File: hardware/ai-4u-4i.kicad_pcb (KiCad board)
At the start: 4 copper layers, 100 x 85 mm, 207 parts, among them J101 TNG-Power-TOP, J102 TNG-Power-BTM, J103 TNG-Data-TOP, J104 TNG-Data-BTM, P102 Debug, P103 PE, P201 INPUT0, P202 INPUT1, P203 INPUT2, P204 INPUT3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

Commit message: fix values
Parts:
- C127, C128: value 4.7nF/2kV -> 1nF/2kV
- R101: value 510 -> 1k

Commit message: specify value
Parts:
- C115: value TBD -> 2.2uF

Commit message: specify value
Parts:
- R253: value TBD -> 1k

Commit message: part specification
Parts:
- R256, R257: value TBD -> DNP

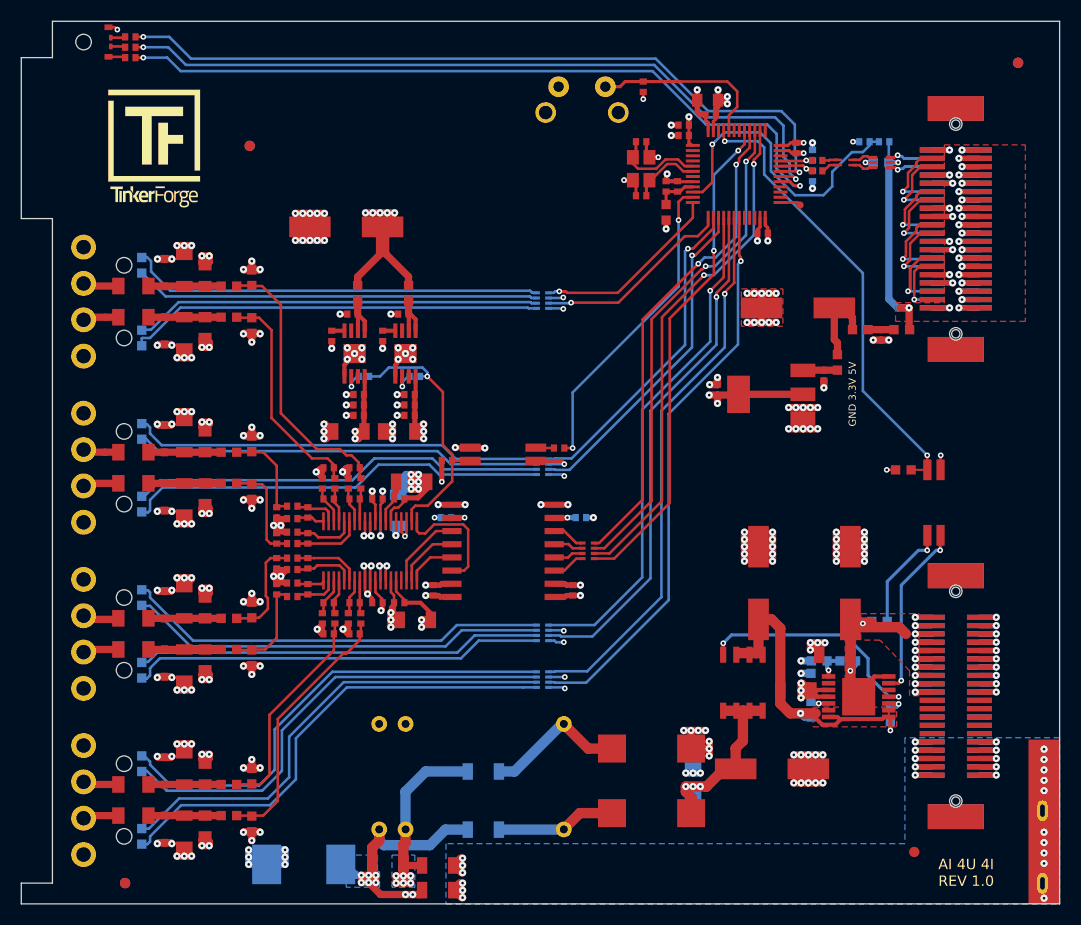
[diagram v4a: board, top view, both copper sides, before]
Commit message: add version 1.1  * fix footprints, improve routing
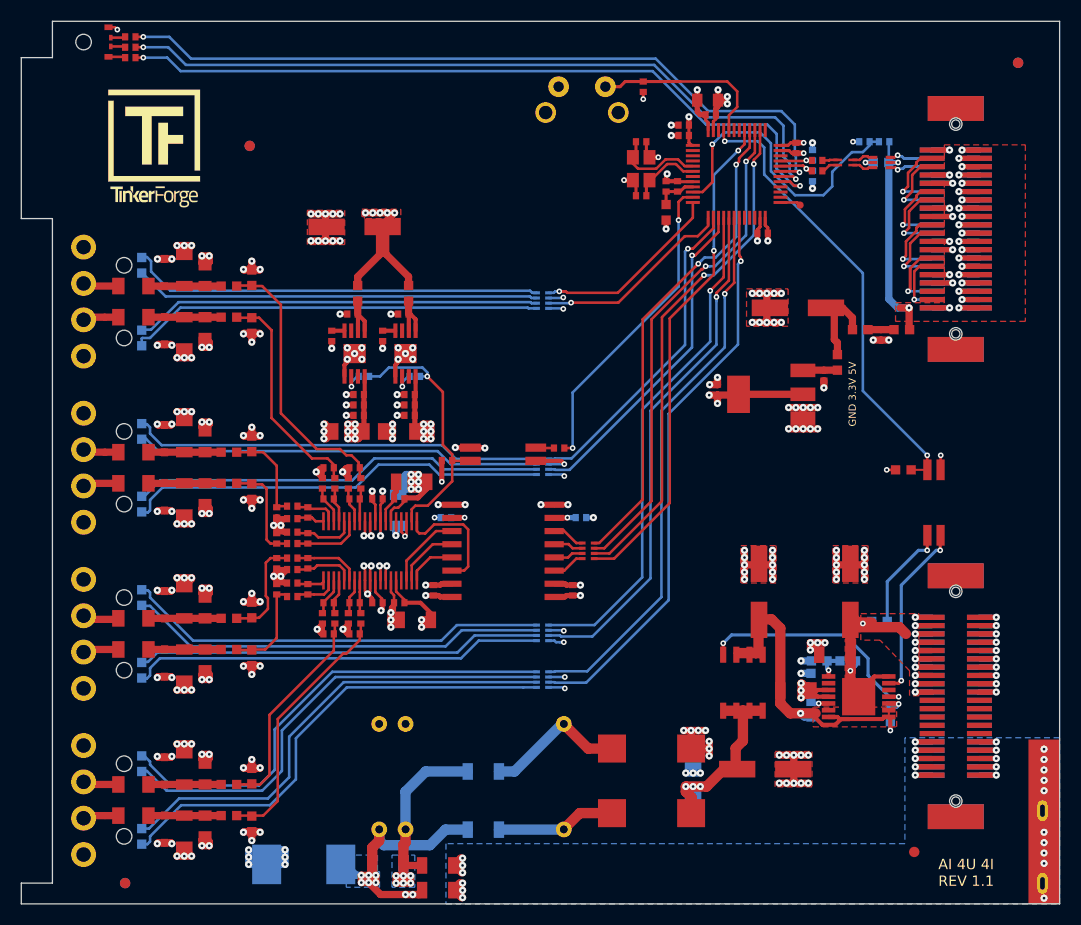
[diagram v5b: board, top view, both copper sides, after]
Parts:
- C108, C109: value TBD -> 33pF
- C111: value TBD -> 100µF; footprint kicad-libraries:ELKO_83 -> kicad-libraries:ELKO_63
- C122, C123, C124, C234: footprint kicad-libraries:ELKO_83 -> kicad-libraries:ELKO_63
- X101: value TBD -> 8MHz
- moved C124 0.85 mm to (160.8, 117.5)
- moved C122 0.85 mm to (169.7, 117.5)
- moved C234 0.80 mm to (121.9, 82.3)
- moved C123 0.65 mm to (161.4, 134.5)
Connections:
- J101 pad 21: (no net) -> Net-(J101-Pad21)
- J101 pad 22: (no net) -> Net-(J101-Pad22)
- J101 pad 23: (no net) -> Net-(J101-Pad23)
- J101 pad 24: (no net) -> Net-(J101-Pad24)
- J101 pad 25: (no net) -> Net-(J101-Pad25)
- J101 pad 26: (no net) -> Net-(J101-Pad26)
- J101 pad 27: (no net) -> Net-(J101-Pad27)
- J101 pad 28: (no net) -> Net-(J101-Pad28)
- J101 pad 29: (no net) -> Net-(J101-Pad29)
- J101 pad 30: (no net) -> Net-(J101-Pad30)
- J102 pad 21: (no net) -> Net-(J102-Pad21)
- J102 pad 22: (no net) -> Net-(J102-Pad22)
- J102 pad 23: (no net) -> Net-(J102-Pad23)
- J102 pad 24: (no net) -> Net-(J102-Pad24)
- J102 pad 25: (no net) -> Net-(J102-Pad25)
- J102 pad 26: (no net) -> Net-(J102-Pad26)
- J102 pad 27: (no net) -> Net-(J102-Pad27)
- J102 pad 28: (no net) -> Net-(J102-Pad28)
- J102 pad 29: (no net) -> Net-(J102-Pad29)
- J102 pad 30: (no net) -> Net-(J102-Pad30)
- J103 pad 35: (no net) -> Net-(J103-Pad35)
- J103 pad 37: (no net) -> Net-(J103-Pad37)
- U101 pad 2: (no net) -> Net-(U101-Pad2)
- U101 pad 20: (no net) -> Net-(U101-Pad20)
- U101 pad 21: (no net) -> Net-(U101-Pad21)
- U101 pad 22: (no net) -> Net-(U101-Pad22)
- U101 pad 26: (no net) -> Net-(U101-Pad26)
- U101 pad 27: (no net) -> Net-(U101-Pad27)
- U101 pad 28: (no net) -> Net-(U101-Pad28)
- U101 pad 3: (no net) -> Net-(U101-Pad3)
- U101 pad 34: (no net) -> Net-(U101-Pad34)
- U101 pad 37: (no net) -> Net-(U101-Pad37)
- U101 pad 4: (no net) -> Net-(U101-Pad4)
- U101 pad 42: (no net) -> Net-(U101-Pad42)
- U101 pad 43: (no net) -> Net-(U101-Pad43)
- U101 pad 46: (no net) -> Net-(U101-Pad46)
- U101 pad 7: (no net) -> Net-(U101-Pad7)
- U104 pad 7: (no net) -> Net-(U104-Pad7)
- U104 pad 8: (no net) -> Net-(U104-Pad8)
- U106 pad 12: (no net) -> Net-(U106-Pad12)
- U106 pad 2: (no net) -> Net-(U106-Pad2)
- U201 pad 35: (no net) -> Net-(U201-Pad35)
- U204 pad 3: (no net) -> Net-(U204-Pad3)
- U204 pad 7: (no net) -> Net-(U204-Pad7)
- U205 pad 3: (no net) -> Net-(U205-Pad3)
- U205 pad 7: (no net) -> Net-(U205-Pad7)
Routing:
- net AVDD: track 35.7 -> 41.1 mm, vias 4 -> 8
- net DVDD: track 45.2 -> 48.7 mm, vias 8 -> 11
- added copper zone on F.Cu, net AGND
- added copper zone on VCC, net AVDD
- added copper zone on VCC, net DVDD
- added copper zone on F.Cu, net VCC
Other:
- board text added: "AI 4U 4I REV 1.1"
- board text added: "Copyright Tinkerforge GmbH 2020. This documentation describes Open Hardware and is licensed under the CERN OHL v. 1.1. You may redistribute and modify this documentation under the terms of the CERN OHL v.1.1. (http://ohwr.org/cernohl). This documentation is distributed WITHOUT ANY EXPRESS OR IMPLIED WARRANTY, INCLUDING OF MERCHANTABILITY, SATISFACTORY QUALITY AND FITNESS FOR A PARTICULAR PURPOSE.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"
- board text removed: "AI 4U 4I REV 1.0"

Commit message: improve routing
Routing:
- net AGND: track 252.6 -> 270.0 mm, vias 160 -> 180
- net DVDD: track 48.7 -> 52.2 mm, vias 11 -> 15
- net AVDD: track 41.1 -> 44.5 mm, vias 8 -> 11
- net GND: track 123.5 -> 124.2 mm, vias 64 -> 65
- net 3V3: track 43.1 -> 43.8 mm, vias 19 -> 20

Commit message: fix text layer
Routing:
- added copper zone on F.Cu, net AGNDA

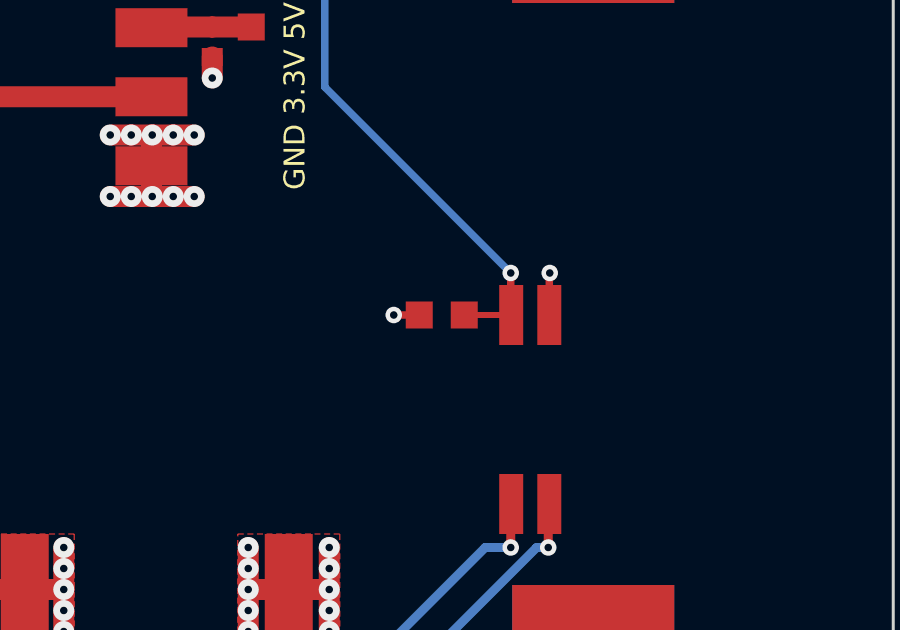
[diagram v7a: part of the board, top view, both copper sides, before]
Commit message: fix footprint
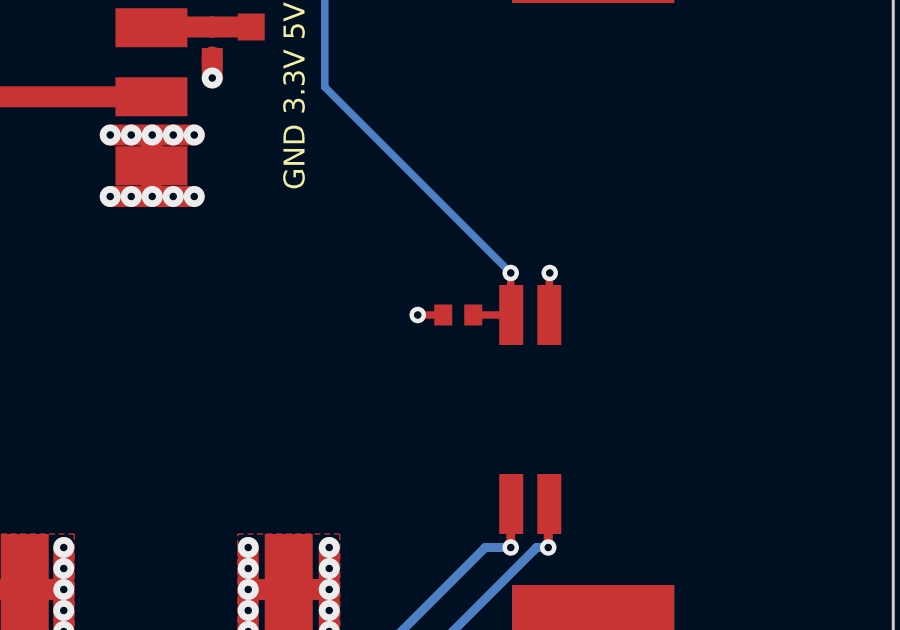
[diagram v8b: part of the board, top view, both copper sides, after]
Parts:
- R109: footprint kicad-libraries:R0603F -> kicad-libraries:R0402F
- moved R109 0.55 mm to (175.3, 105.7)
